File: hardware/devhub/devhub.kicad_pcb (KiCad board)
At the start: 4 copper layers, 169 x 85 mm, 219 parts, among them J1 USB-C PWR IN, J101 USB-C, J2 USB-C UPSTREAM, J201 USB-C, J3 PORTA 7 (scorta), J301 USB-C, J4 SWD, J401 USB-C, J5 Banana COM 1, J501 USB-A, J6 Banana NC 1, J7 Banana COM 2, J8 Banana NC 2, J9 UART debug, K1 G5Q-1 DC5, K2 G5Q-1 DC5, Q101 AO3400A, Q201 AO3400A, Q301 AO3400A, Q401 AO3400A, Q501 AO3400A, SW1 relè on/off, SW101 porta on/off, SW2 relè on/off, SW201 porta on/off, SW301 porta on/off, SW401 porta on/off, SW501 porta on/off, U1 AP7361C-33E, U101 PI3USB4002A, U12 MCP120T-300I/TT, U13 TPS259470ARPWR, U2 USB2517I-JZX, U201 PI3USB4002A, U3 STM32G0B1RET6, U301 PI3USB4002A, U4 TPS2561ADRC, U401 PI3USB4002A, U5 TPS2561ADRC, U501 PI3USB4002A, U6 TPS2561ADRC, U7 INA3221, U8 INA3221, U9 ULN2003V12, Y1 24MHz 12pF

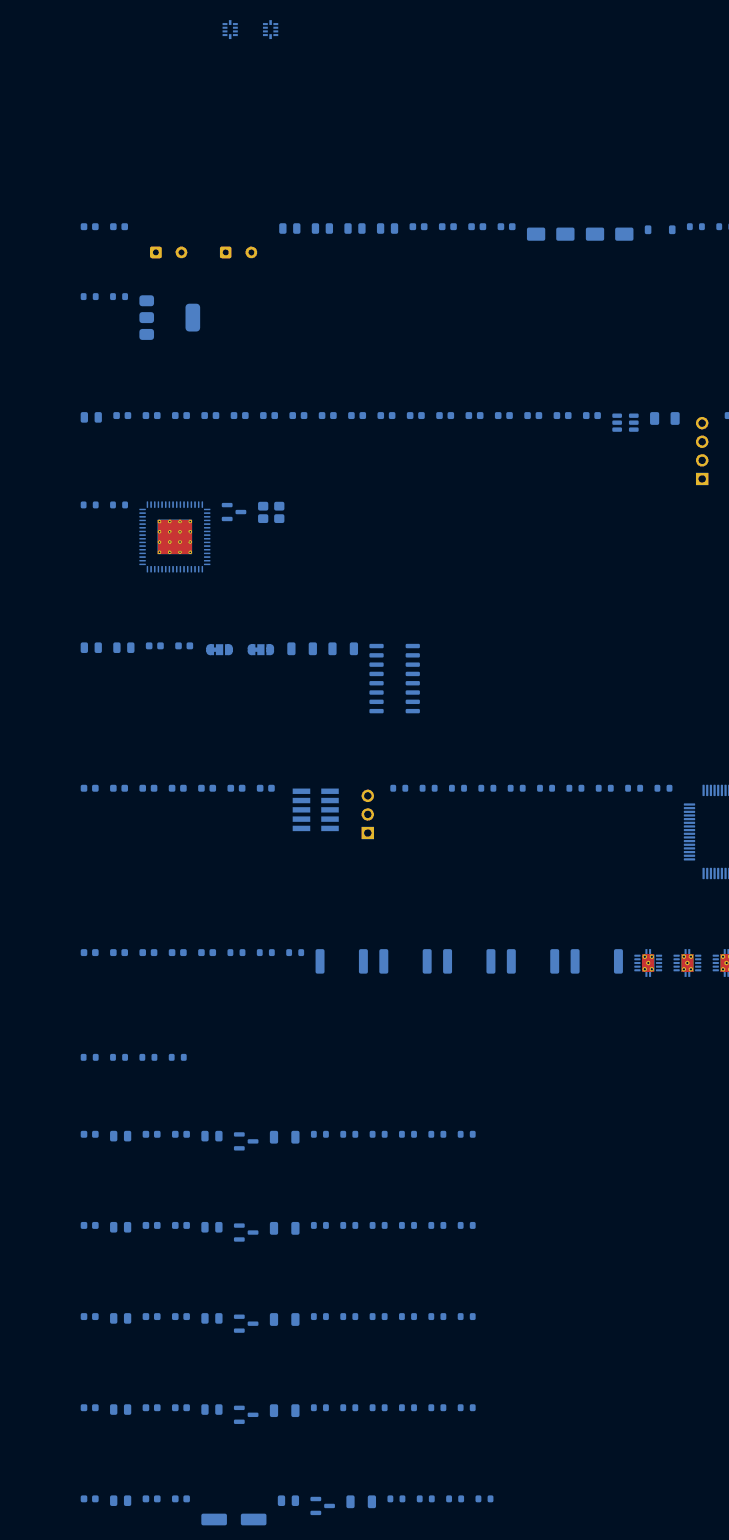
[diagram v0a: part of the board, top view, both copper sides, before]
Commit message: PCB rules in KiCad, USB pair names, eFuse output bypass and U2 thermal vias (D44-D50)
Stackup JLC04161H-7628, netclasses and custom DRC rules (devhub.kicad_dru) from
docs/regole-pcb.md, with a section for the checks that DRC cannot cover. C7 1 uF on
the TPS259470A output before the shunt (D48). USB nets renamed to DP/DN so KiCad
recognizes the differential pairs (D49). U2 footprint with 0.3 mm thermal vias, open
on both sides for the prototype; encroached vias and a JLCPCB order note for
production (D50). Also includes stock part codes, cost comparison and placement rules
(D44-D47).
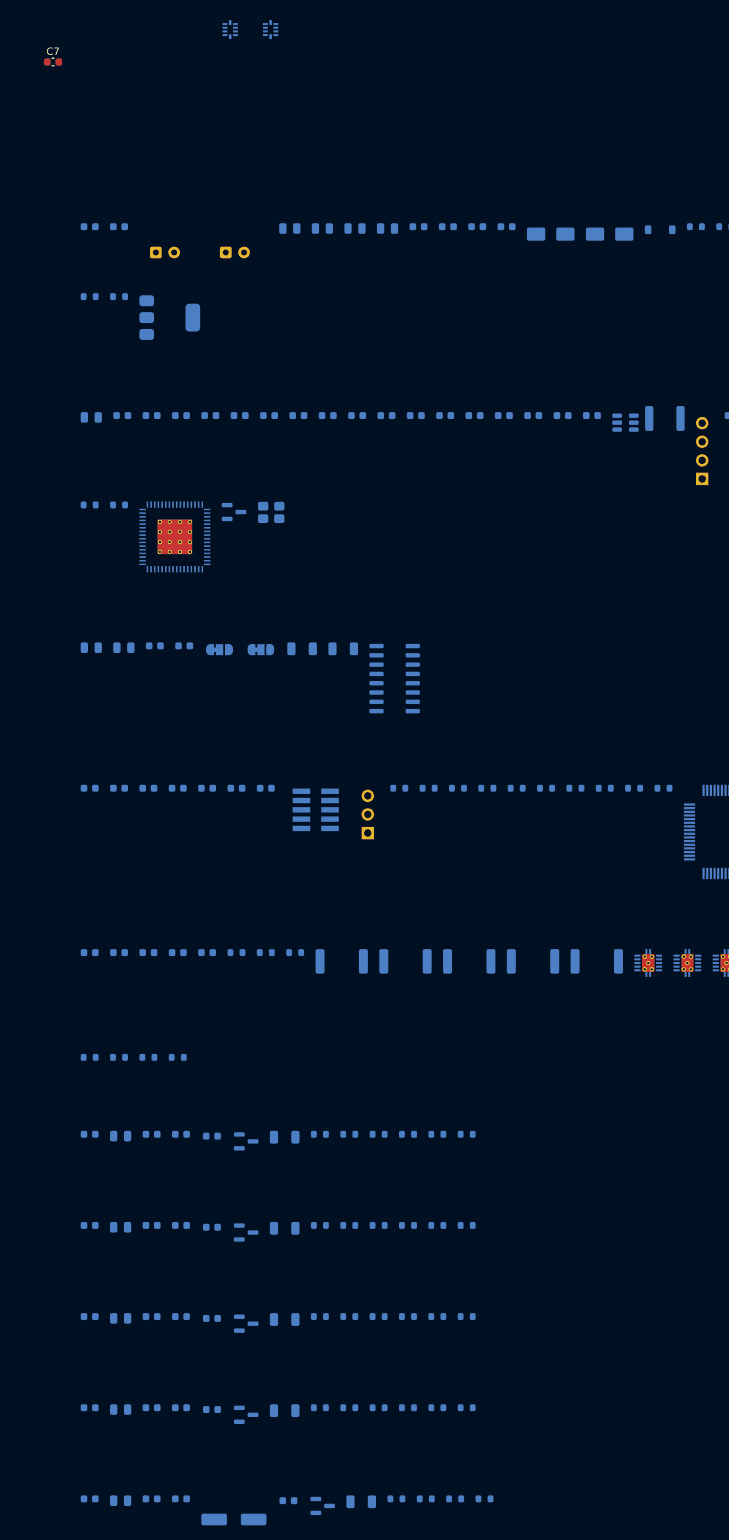
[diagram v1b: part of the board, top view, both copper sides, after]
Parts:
- added C7: 1u 25V, Capacitor_SMD:C_0603_1608Metric, F.Cu at (240.5, 43.8)
- C106, C206, C306, C406, C506: footprint Capacitor_SMD:C_0805_2012Metric -> Capacitor_SMD:C_0603_1608Metric
- C3, C4: footprint Capacitor_THT:CP_Radial_D8.0mm_P3.50mm -> Capacitor_THT:CP_Radial_D6.3mm_P2.50mm
- C505: footprint Capacitor_SMD:CP_Elec_6.3x7.7 -> Capacitor_SMD:CP_Elec_6.3x5.8
- F1: footprint Fuse:Fuse_1206_3216Metric -> Fuse:Fuse_1812_4532Metric
- U2: footprint Package_DFN_QFN:QFN-64-1EP_9x9mm_P0.5mm_EP4.7x4.7mm_ThermalVias -> lcsc_footprints:QFN-64-1EP_9x9mm_P0.5mm_EP4.7x4.7mm_ThermalVias_0.3mm
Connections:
- net /Hub USB2517/SPARE_DM renamed /Hub USB2517/SPARE_DN
- net /Hub USB2517/UP_DM_C renamed /Hub USB2517/UP_CONN_DN
- net /Hub USB2517/UP_DP_C renamed /Hub USB2517/UP_CONN_DP
- net /Hub USB2517/USBUP_DM renamed /Hub USB2517/USBUP_DN
- net /Porta 1 (USB-C)/DM_C renamed /Porta 1 (USB-C)/CONN_DN
- net /Porta 1 (USB-C)/DP_C renamed /Porta 1 (USB-C)/CONN_DP
- net /Porta 2 (USB-C)/DM_C renamed /Porta 2 (USB-C)/CONN_DN
- net /Porta 2 (USB-C)/DP_C renamed /Porta 2 (USB-C)/CONN_DP
- net /Porta 3 (USB-C)/DM_C renamed /Porta 3 (USB-C)/CONN_DN
- net /Porta 3 (USB-C)/DP_C renamed /Porta 3 (USB-C)/CONN_DP
- net /Porta 4 (USB-C)/DM_C renamed /Porta 4 (USB-C)/CONN_DN
- net /Porta 4 (USB-C)/DP_C renamed /Porta 4 (USB-C)/CONN_DP
- net /Porta 5 (USB-A)/DM_C renamed /Porta 5 (USB-A)/CONN_DN
- net /Porta 5 (USB-A)/DP_C renamed /Porta 5 (USB-A)/CONN_DP
- net HUB_DM1 renamed HUB_DN1
- net HUB_DM2 renamed HUB_DN2
- net HUB_DM3 renamed HUB_DN3
- net HUB_DM4 renamed HUB_DN4
- net HUB_DM5 renamed HUB_DN5
- net USB_MCU_DM renamed USB_MCU_DN

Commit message: Review 03 fixes and PCB placement update (D51-D56)
Schematic review 03 (docs/lavorazioni/review_03.md):
- D1 SMAJ20A was reversed (cathode on GND): rotated, and replaced by a project
  symbol devhub:SMAJ20A with explicit K/A pin names; breakdown corrected to
  22.2-24.5 V (R03-01).
- D21 BAT54WS from VBUS_DET to 3V3 keeps USB2517 pin 44 within VDD33 + 0.5 V
  when the hub is unpowered (D53, R03-02).
- USB-A port limited to 1.5 A, the J501 connector rating: R62 33.2k, RF-5
  updated (D54, R03-03).
- RF-6 accuracy relaxed to 2 mA + 5 % because of the thick-film shunt TCR
  (D55, R03-04).
- Courtyards of the LCSC U13 and PI3USB4002A footprints enlarged to cover the
  pads, also in the PCB copies (R03-05).
- LDO U1 kept (buck rejected); GND heatsink zone and 10 vias on its tab, thermal
  budget corrected to 0.8-0.9 W worst case (D56).

PCB: connector layout (D51), USB pair polarity on the bottom side (D52), relays
moved with the contact keepout areas redrawn, D21 placed next to C21. Cost
comparison updated with D21 and R62.
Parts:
- added D21: BAT54WS, Diode_SMD:D_SOD-323, B.Cu at (208.8, 79.0)
- C7: moved to B.Cu
- R62: value 24.3k 1% -> 33.2k 1%
- moved R32 246.6 mm to (114.8, 79.6), turned to 90 degrees
- moved R31 240.9 mm to (116.5, 79.6), turned to 90 degrees
- moved R30 235.2 mm to (118.2, 79.6), turned to 90 degrees
- moved R2 223.7 mm to (108.8, 74.0), turned to 90 degrees
- moved R1 217.9 mm to (110.6, 74.0), turned to 90 degrees
- moved R5 215.5 mm to (131.5, 79.5)
- moved D2 209.5 mm to (108.0, 87.5)
- moved D4 207.1 mm to (117.0, 83.6)
- moved C10 197.1 mm to (93.6, 76.6), turned to 90 degrees
- moved U9 195.5 mm to (95.1, 91.5), turned to 90 degrees
- moved R507 194.8 mm to (141.5, 126.0), turned to 90 degrees
- moved C9 190.7 mm to (95.8, 76.6), turned to 90 degrees
- moved D1 190.6 mm to (118.0, 74.0)
- moved R506 189.5 mm to (141.5, 129.5), turned to 90 degrees
- moved U8 189.2 mm to (165.0, 108.0)
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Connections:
- D1 pad 1: GND -> /Alimentazione/VBUS_IN
- D1 pad 2: /Alimentazione/VBUS_IN -> GND
- D20 pad 1: /Hub USB2517/UP_CONN_DP -> /Hub USB2517/UP_CONN_DN
- D20 pad 3: /Hub USB2517/UP_CONN_DN -> /Hub USB2517/UP_CONN_DP
- D20 pad 4: /Hub USB2517/USBUP_DN -> /Hub USB2517/USBUP_DP
- D20 pad 6: /Hub USB2517/USBUP_DP -> /Hub USB2517/USBUP_DN
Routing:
- net HUB_DN1: track 0.00 -> 61.8 mm
- net HUB_DP1: track 0.00 -> 61.8 mm
- net HUB_DN5: track 0.00 -> 61.5 mm
- net HUB_DP5: track 0.00 -> 61.5 mm
- net HUB_DN2: track 0.00 -> 48.1 mm
- net HUB_DP2: track 0.00 -> 48.1 mm
- net HUB_DP4: track 0.00 -> 46.5 mm
- net HUB_DN4: track 0.00 -> 46.5 mm
- net USB_MCU_DP: track 0.00 -> 38.8 mm
- net USB_MCU_DN: track 0.00 -> 37.6 mm, vias 0 -> 2
- net HUB_DP3: track 0.00 -> 35.2 mm
- net HUB_DN3: track 0.00 -> 35.2 mm
- net /Hub USB2517/SPARE_DP: track 0.00 -> 27.6 mm
- net /Hub USB2517/SPARE_DN: track 0.00 -> 26.9 mm
- net /Hub USB2517/USBUP_DP: track 0.00 -> 19.6 mm
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- added copper zone on B.Cu, net GND
- added copper zone on In2.Cu, net GND

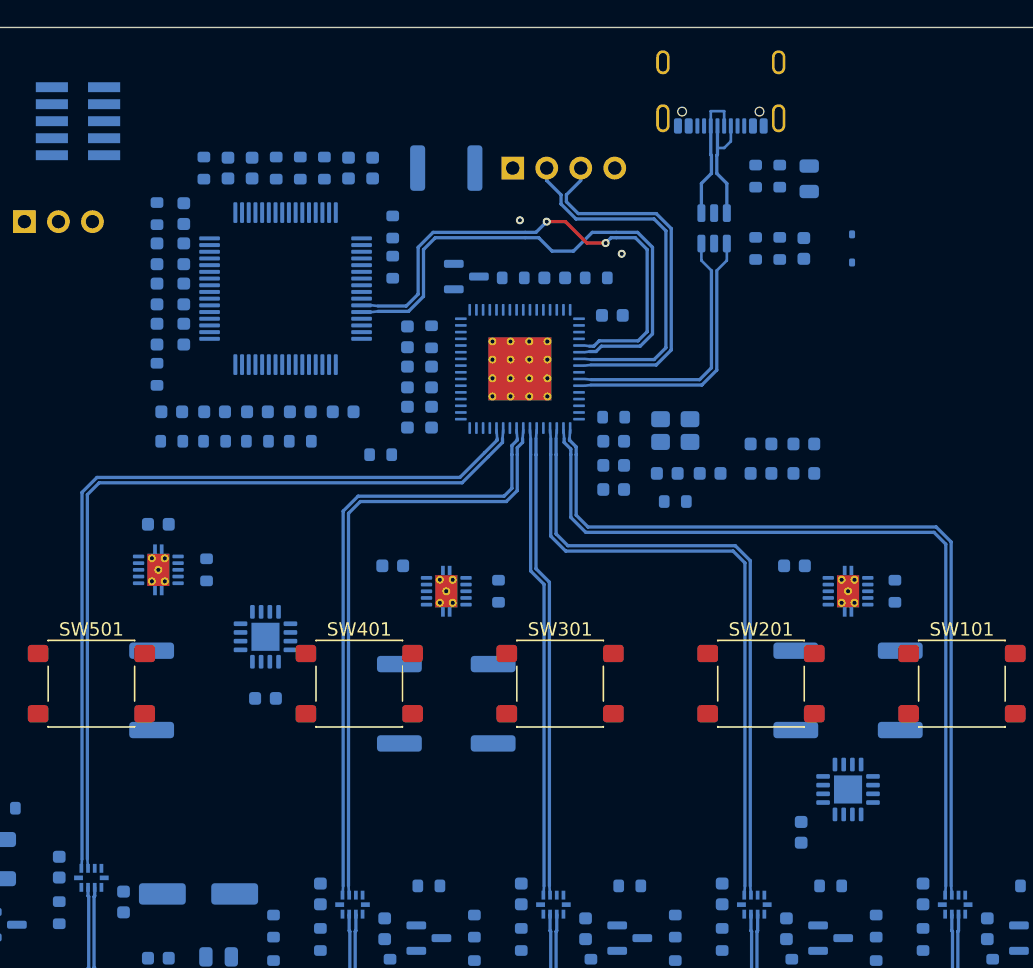
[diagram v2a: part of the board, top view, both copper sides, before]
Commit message: MCU and hub decoupling, USB2517 checklist, VBUS_DET without clamp diode (D53, D57, D58)
- MCU U3 decoupling per DS13560 fig. 15: C41 100 nF + C40 4.7 uF on VDD/VSS,
  C42 100 nF on VREF+; C43, C44 and C45 removed (D57).
- Hub U2 decoupling per the Microchip USB2517 Hardware Design Checklist: 100 nF on
  each 3.3 V pin (C38 added), 1 uF shared by VDDA33 (C31) and on VDD33CR, only 1 uF
  on VDD18 and VDD18PLL (C34, C36 removed). Each capacitor drawn on its pin's wire.
  The 100 nF of U2 and U12 are 0402 (stock ID 217) to fit next to the pins between
  the USB pairs; DRC exception for the +3V3 stubs inside the U2_DECAP areas (D58).
- VBUS_DET: D21 removed, plain 100k/100k divider as recommended by the checklist
  (D53, R03-02 closed).
- USB-C connector exits without tuning meanders: the ~2.3 mm D+/D- difference of the
  pad crossing is accepted; looser skew limit on the connector-side nets.
- PCB: relay contact keepouts redrawn, U2 fanout and decoupling placement, zone refill.
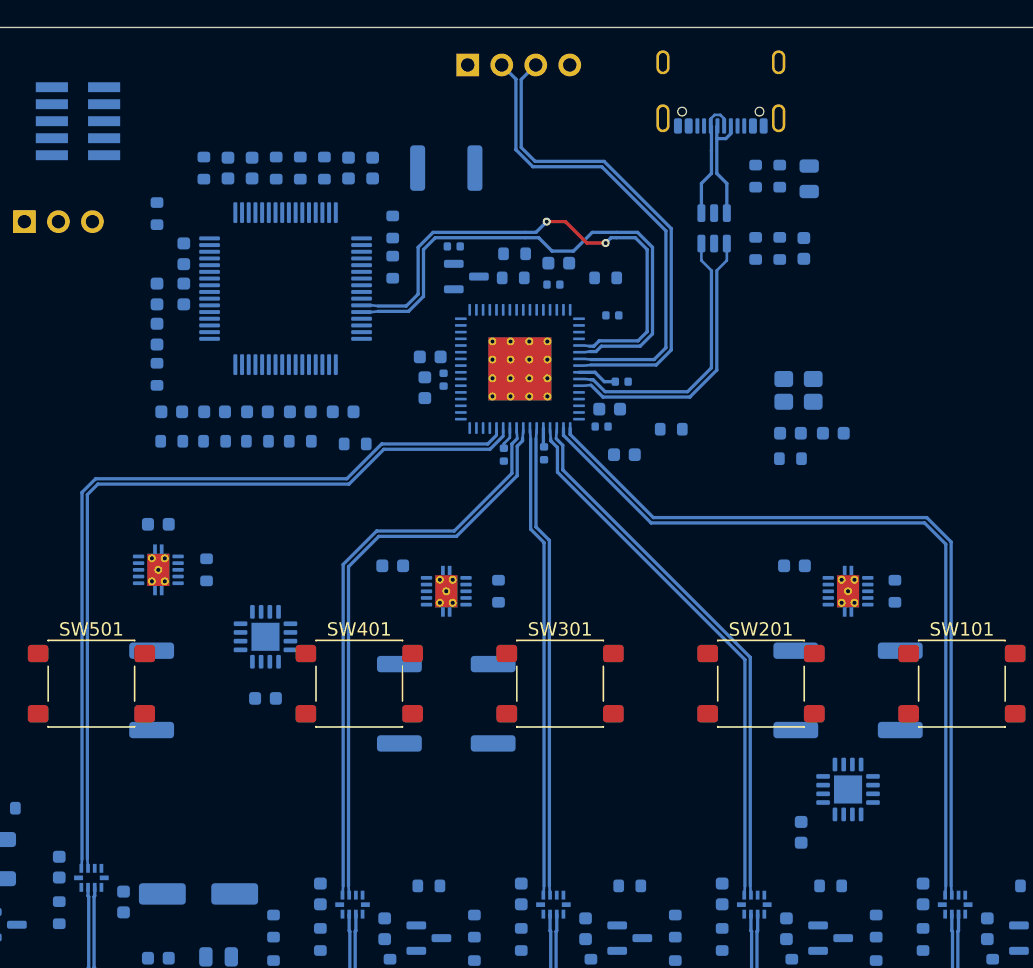
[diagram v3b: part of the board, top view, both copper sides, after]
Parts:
- removed C34, C36, C43, C44: 100n, Capacitor_SMD:C_0603_1608Metric
- removed C45: 1u, Capacitor_SMD:C_0603_1608Metric
- removed D21: BAT54WS, Diode_SMD:D_SOD-323
- added C38: 100n, Capacitor_SMD:C_0402_1005Metric, B.Cu at (182.8, 94.4)
- C25, C26, C27, C28, C29, C30, C37: footprint Capacitor_SMD:C_0603_1608Metric -> Capacitor_SMD:C_0402_1005Metric
- moved C32 29.0 mm to (176.9, 89.4), turned to -90 degrees
- moved C29 24.2 mm to (178.3, 88.8), turned to -90 degrees
- moved C37 21.7 mm to (179.1, 78.8), turned to 180 degrees
- moved C26 16.0 mm to (191.6, 89.0), turned to 0 degrees
- moved C30 15.2 mm to (190.1, 92.3)
- moved C24 12.6 mm to (186.9, 80.1), turned to 0 degrees
- moved C25 10.6 mm to (185.8, 94.3), turned to -90 degrees
- moved C31 10.3 mm to (191.8, 94.4)
- moved C23 9.68 mm to (207.4, 92.8)
- moved Y1 9.68 mm to (204.8, 89.6)
- moved C22 9.68 mm to (204.2, 92.8)
- moved R24 9.18 mm to (204.2, 94.7)
- moved R28 8.77 mm to (183.6, 79.4), turned to 0 degrees
- moved J3 8.40 mm to (180.1, 65.3)
- moved R25 4.39 mm to (195.3, 92.5)
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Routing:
- net /Hub USB2517/SPARE_DP: track 27.6 -> 36.3 mm
- net /Hub USB2517/SPARE_DN: track 26.9 -> 35.6 mm
- net HUB_DP2: track 48.1 -> 40.8 mm
- net HUB_DN2: track 48.1 -> 40.8 mm
- net +3V3: track 0.00 -> 6.12 mm
- net HUB_DP1: track 61.8 -> 58.7 mm
- net HUB_DN4: track 46.5 -> 43.5 mm
- net HUB_DP4: track 46.5 -> 43.5 mm
- net HUB_DN1: track 61.8 -> 58.8 mm
- net /Hub USB2517/USBUP_DN: track 18.9 -> 19.7 mm
- net /Hub USB2517/USBUP_DP: track 19.6 -> 20.4 mm
- net GND: vias 12 -> 10

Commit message: wip pcb
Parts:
- moved C504 29.3 mm to (143.9, 79.6), turned to 180 degrees
- moved C304 20.4 mm to (145.0, 84.8), turned to 180 degrees
- moved R4 17.8 mm to (148.7, 68.2)
- moved J9 17.3 mm to (159.8, 65.4)
- moved C204 16.9 mm to (145.0, 86.3), turned to 180 degrees
- moved C3 16.8 mm to (128.0, 65.3)
- moved C4 16.8 mm to (128.0, 72.8)
- moved R3 15.6 mm to (145.6, 68.2)
- moved C40 15.1 mm to (142.3, 81.5), turned to 180 degrees
- moved R45 14.8 mm to (154.6, 73.0)
- moved C104 13.4 mm to (145.0, 87.9), turned to 180 degrees
- moved C2 13.1 mm to (151.7, 68.4)
- moved R42 12.4 mm to (144.5, 76.1), turned to 180 degrees
- moved C46 11.8 mm to (147.1, 80.0), turned to 180 degrees
- moved J4 11.8 mm to (139.4, 67.4)
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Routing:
- net EN_P1: track 0.00 -> 137.5 mm, vias 0 -> 4
- net OE_N_P1: track 0.00 -> 121.8 mm, vias 0 -> 1
- net DIS_P1: track 0.00 -> 113.6 mm, vias 0 -> 1
- net LED_HOST: track 0.00 -> 97.6 mm, vias 0 -> 1
- net GND: track 0.00 -> 92.5 mm, vias 10 -> 102
- net SDA: track 0.00 -> 84.5 mm, vias 0 -> 2
- net SCL: track 0.00 -> 79.8 mm, vias 0 -> 2
- net VBUS_P3: track 0.00 -> 63.2 mm, vias 0 -> 12
- net INA_ALERT: track 0.00 -> 53.9 mm, vias 0 -> 4
- net EN_P2: track 0.00 -> 46.5 mm, vias 0 -> 2
- net VBUS_P2: track 0.00 -> 45.6 mm, vias 0 -> 12
- net VBUS_P1: track 0.00 -> 42.8 mm, vias 0 -> 10
- net FAULT_P1: track 0.00 -> 42.4 mm, vias 0 -> 2
- net /Load switch e misura corrente/SW_OUT_P3: track 0.00 -> 40.3 mm, vias 0 -> 2
- net FAULT_P2: track 0.00 -> 37.8 mm, vias 0 -> 2
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- added copper zone on B.Cu, net +3V3
- added copper zone on In1.Cu, net +3V3
- added copper zone on B.Cu, net +5V
- added copper zone on F.Cu, net GND
- added copper zone on B.Cu, net VBUS_P1
- added copper zone on In1.Cu, net VBUS_P1
- added copper zone on B.Cu, net VBUS_P2
- added copper zone on In1.Cu, net VBUS_P2
- added copper zone on B.Cu, net VBUS_P3
- added copper zone on In1.Cu, net VBUS_P3
- added copper zone on B.Cu, net VBUS_P4
- added copper zone on In1.Cu, net VBUS_P4
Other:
- board size 169 x 85 mm -> 172.5 x 85 mm
